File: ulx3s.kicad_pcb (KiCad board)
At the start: 4 copper layers, 94 x 50.8 mm, 164 parts, among them J3 WIFI_OFF, J4 CONN_02X03, Q1 BC857, Q2 2N7002, U10 IS25LP128F-JBLE, U11 PCA9306D, U3 TLV62569DBV, U4 TLV62569DBV, U5 TLV62569DBV, U7 MCP7940NT, Y2 32768Hz

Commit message: full breakout
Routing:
- net Net-(U1-PadD11): track 0.00 -> 3.33 mm, vias 0 -> 1
- net Net-(U1-PadD10): track 0.00 -> 3.17 mm, vias 0 -> 1
- net +3V3: track 14.5 -> 12.0 mm
- net FPDI_SCL: track 6.41 -> 4.93 mm
- net GND: track 23.8 -> 22.4 mm
- net GN27: track 5.26 -> 4.13 mm
- net 2V5_3V3: track 4.11 -> 3.06 mm
- net +1V1: track 13.6 -> 14.5 mm, vias 11 -> 13
- net WIFI_GPIO25: track 4.93 -> 5.73 mm
- net GN0: track 3.17 -> 2.37 mm
- net +2V5: track 6.93 -> 6.18 mm
- net SW4: track 4.81 -> 4.13 mm
- net Net-(U1-PadE11): track 4.81 -> 4.13 mm

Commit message: finishing touches to bga breakout
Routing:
- net +3V3: track 12.0 -> 7.48 mm
- net Net-(U1-PadR3): track 0.00 -> 2.77 mm, vias 0 -> 1
- net ADC_MOSI: track 5.25 -> 6.39 mm
- net SD_WP: track 5.66 -> 4.54 mm
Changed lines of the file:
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@@
     (thickness 1.6)
     (drawings 5)
-    (tracks 810)
+    (tracks 806)
     (zones 0)
     (modules 228)
@@
   )
   (setup
-    (last_trace_width 0.4)
+    (last_trace_width 0.127)
     (user_trace_width 0.127)
     (user_trace_width 0.2)
@@
   )
   (module Capacitor_SMD:C_0603_1608Metric (layer B.Cu)
-    (at 131.08 95.175 270)
+    (at 131.28 95.175 270)
     (descr "Capacitor SMD 0603 (1608 Metric), square (rectangular) end terminal, IPC_7351 nominal, (Body size source: IPC-SM-782 page 76, https://www.pcb-3d.com/wordpress/wp-content/uploads/ipc-sm-782a_amendment_1_and_2.pdf), generated with kicad-footprint-generator")
     (tags capacitor)
@@
   (via (at 134.88 91.4) (size 0.419) (drill 0.2) (layers F.Cu B.Cu) (net 1))
   (segment (start 134.88 90.75) (end 134.88 91.4) (width 0.2) (layer B.Cu) (net 1))
-  (via (at 130.88 96.6) (size 0.419) (drill 0.2) (layers F.Cu B.Cu) (net 1))
   (via (at 135.68 96.2) (size 0.419) (drill 0.2) (layers F.Cu B.Cu) (net 1))
   (via (at 136.48 96) (size 0.419) (drill 0.2) (layers F.Cu B.Cu) (net 1))
@@
   (segment (start 132.88 95.6) (end 133.28 96) (width 0.4) (layer B.Cu) (net 1))
   (segment (start 132.88 95.375) (end 132.88 95.6) (width 0.4) (layer B.Cu) (net 1))
-  (segment (start 131.08 96.4) (end 130.88 96.6) (width 0.4) (layer B.Cu) (net 1))
-  (segment (start 131.08 95.95) (end 131.08 96.4) (width 0.4) (layer B.Cu) (net 1))
   (segment (start 135.23 95.75) (end 135.68 96.2) (width 0.4) (layer B.Cu) (net 1))
   (segment (start 134.88 95.75) (end 135.23 95.75) (width 0.4) (layer B.Cu) (net 1))
@@
   (segment (start 136.88 95.375) (end 136.88 95.6) (width 0.4) (layer B.Cu) (net 1))
   (segment (start 132.08 90.2) (end 132.48 90.6) (width 0.4) (layer F.Cu) (net 1))
+  (via (at 131.68 96.6) (size 0.419) (drill 0.2) (layers F.Cu B.Cu) (net 1))
+  (segment (start 131.28 96.2) (end 131.68 96.6) (width 0.4) (layer B.Cu) (net 1))
+  (segment (start 131.28 95.95) (end 131.28 96.2) (width 0.4) (layer B.Cu) (net 1))
   (via (at 134.08 93) (size 0.419) (drill 0.2) (layers F.Cu B.Cu) (net 5))
   (via (at 131.68 91.4) (size 0.419) (drill 0.2) (layers F.Cu B.Cu) (net 5))
@@
   (segment (start 128.48 95.4) (end 128.88 95) (width 0.2) (layer F.Cu) (net 5))
   (segment (start 128.08 95.8) (end 128.48 95.4) (width 0.2) (layer F.Cu) (net 5))
-  (via (at 128.48 95.4) (size 0.419) (drill 0.2) (layers F.Cu B.Cu) (net 5))
-  (segment (start 130.995338 93.54799) (end 131.48 93.063328) (width 0.2) (layer B.Cu) (net 5))
-  (segment (start 130.781968 93.54799) (end 130.995338 93.54799) (width 0.2) (layer B.Cu) (net 5))
-  (segment (start 130.60613 93.372152) (end 130.781968 93.54799) (width 0.2) (layer B.Cu) (net 5))
-  (segment (start 129.879132 93.372152) (end 130.60613 93.372152) (width 0.2) (layer B.Cu) (net 5))
-  (segment (start 128.48352 94.767764) (end 129.879132 93.372152) (width 0.2) (layer B.Cu) (net 5))
-  (segment (start 128.48352 95.39648) (end 128.48352 94.767764) (width 0.2) (layer B.Cu) (net 5))
-  (segment (start 128.48 95.4) (end 128.48352 95.39648) (width 0.2) (layer B.Cu) (net 5))
   (segment (start 135.68 87.6) (end 135.68 87.4) (width 0.2) (layer B.Cu) (net 5))
   (segment (start 134.88 88.85) (end 134.88 88.4) (width 0.2) (layer B.Cu) (net 5))
@@
   (segment (start 131.28 91.8) (end 132.08 91) (width 0.2) (layer F.Cu) (net 5))
   (segment (start 131.28 91) (end 131.68 91.4) (width 0.2) (layer F.Cu) (net 5))
+  (via (at 128.48 95.4) (size 0.419) (drill 0.2) (layers F.Cu B.Cu) (net 5))
   (segment (start 127.28 96.6) (end 126.28 96.6) (width 0.127) (layer F.Cu) (net 6))
   (segment (start 127.28 94.2) (end 126.28 94.2) (width 0.127) (layer F.Cu) (net 7))
@@
   (via (at 130.08 95.4) (size 0.419) (drill 0.2) (layers F.Cu B.Cu) (net 19))
   (segment (start 130.48 95) (end 130.08 95.4) (width 0.127) (layer F.Cu) (net 19))
-  (segment (start 130.08 95.4) (end 130.08 99.2) (width 0.127) (layer B.Cu) (net 19))
+  (segment (start 130.08 95.4) (end 130.08 99.2) (width 0.127) (layer In2.Cu) (net 19))
   (segment (start 130.070501 96.209499) (end 130.070501 99.190501) (width 0.127) (layer F.Cu) (net 20))
   (segment (start 130.48 95.8) (end 130.070501 96.209499) (width 0.127) (layer F.Cu) (net 20))
@@
   (segment (start 139.670501 96.190501) (end 139.670501 99.190501) (width 0.127) (layer F.Cu) (net 140))
   (segment (start 139.28 95.8) (end 139.670501 96.190501) (width 0.127) (layer F.Cu) (net 140))
-  (via (at 139.679999 94.6) (size 0.419) (drill 0.2) (layers F.Cu B.Cu) (net 141))
-  (segment (start 139.28 94.200001) (end 139.679999 94.6) (width 0.127) (layer F.Cu) (net 141))
   (segment (start 139.28 94.2) (end 139.28 94.200001) (width 0.127) (layer F.Cu) (net 141))
+  (segment (start 139.28 94.200001) (end 139.679999 94.6) (width 0.127) (layer F.Cu) (net 141))
+  (via (at 139.679999 94.6) (size 0.419) (drill 0.2) (layers F.Cu B.Cu) (net 141))
+  (segment (start 137.68 95.58766) (end 137.68 99) (width 0.127) (layer B.Cu) (net 141))
+  (segment (start 138.06766 95.2) (end 137.68 95.58766) (width 0.127) (layer B.Cu) (net 141))
+  (segment (start 139.08 95.2) (end 138.06766 95.2) (width 0.127) (layer B.Cu) (net 141))
+  (segment (start 139.679999 94.600001) (end 139.08 95.2) (width 0.127) (layer B.Cu) (net 141))
   (segment (start 139.679999 94.6) (end 139.679999 94.600001) (width 0.127) (layer B.Cu) (net 141))
-  (segment (start 139.679999 94.600001) (end 139.48 94.8) (width 0.127) (layer B.Cu) (net 141))
-  (segment (start 139.48 94.8) (end 139.48 99.2) (width 0.127) (layer B.Cu) (net 141))
   (via (at 140.48 94.6) (size 0.419) (drill 0.2) (layers F.Cu B.Cu) (net 142))
   (segment (start 140.08 94.2) (end 140.48 94.6) (width 0.127) (layer F.Cu) (net 142))
@@
   (via (at 139.68 93.8) (size 0.419) (drill 0.2) (layers F.Cu B.Cu) (net 143))
   (segment (start 140.08 93.4) (end 139.68 93.8) (width 0.127) (layer F.Cu) (net 143))
-  (segment (start 139.73401 98.14599) (end 139.73401 99.05401) (width 0.127) (layer B.Cu) (net 143))
-  (segment (start 139.73401 95.14599) (end 139.73401 98.14599) (width 0.127) (layer B.Cu) (net 143))
-  (segment (start 140.079999 94.800001) (end 139.73401 95.14599) (width 0.127) (layer B.Cu) (net 143))
   (segment (start 140.079999 94.200001) (end 140.079999 94.800001) (width 0.127) (layer B.Cu) (net 143))
   (segment (start 139.68 93.8) (end 140.079999 94.200001) (width 0.127) (layer B.Cu) (net 143))
+  (segment (start 140.079999 94.874069) (end 139.68 95.274068) (width 0.127) (layer B.Cu) (net 143))
+  (segment (start 140.079999 94.800001) (end 140.079999 94.874069) (width 0.127) (layer B.Cu) (net 143))
+  (segment (start 139.68 95.274068) (end 139.68 98.8) (width 0.127) (layer B.Cu) (net 143))
   (via (at 131.68 85) (size 0.419) (drill 0.2) (layers F.Cu B.Cu) (net 144))
   (segment (start 132.08 85.4) (end 131.68 85) (width 0.127) (layer F.Cu) (net 144))
@@
   (segment (start 139.292371 94.387629) (end 139.48 94.2) (width 0.127) (layer In2.Cu) (net 275))
   (segment (start 139.48 94.2) (end 143.28 94.2) (width 0.127) (layer In2.Cu) (net 275))
+  (via (at 128.48 94.6) (size 0.419) (drill 0.2) (layers F.Cu B.Cu) (net 276))
+  (segment (start 128.88 94.2) (end 128.48 94.6) (width 0.127) (layer F.Cu) (net 276))
+  (segment (start 128.48 94.6) (end 126.28 94.6) (width 0.127) (layer B.Cu) (net 276))
   (via (at 130.088653 93.808653) (size 0.419) (drill 0.2) (layers F.Cu B.Cu) (net 277))
   (segment (start 130.48 93.417306) (end 130.088653 93.808653) (width 0.127) (layer F.Cu) (net 277))
   (segment (start 130.48 93.4) (end 130.48 93.417306) (width 0.127) (layer F.Cu) (net 277))
-  (segment (start 130.088653 93.808653) (end 129.68 94.217306) (width 0.127) (layer B.Cu) (net 277))
-  (segment (start 129.68 94.217306) (end 129.68 95) (width 0.127) (layer B.Cu) (net 277))
-  (segment (start 129.68 95) (end 128.88 95.8) (width 0.127) (layer B.Cu) (net 277))
-  (segment (start 128.88 95.8) (end 126.28 95.8) (width 0.127) (layer B.Cu) (net 277))
+  (segment (start 130.088653 93.808653) (end 129.697306 94.2) (width 0.127) (layer B.Cu) (net 277))
+  (segment (start 129.697306 94.2) (end 126.28 94.2) (width 0.127) (layer B.Cu) (net 277))
   (via (at 130.88 93) (size 0.419) (drill 0.2) (layers F.Cu B.Cu) (net 278))
   (segment (start 130.48 92.6) (end 130.88 93) (width 0.127) (layer F.Cu) (net 278))
@@
     (polygon
       (pts
-        (xy 137.88 87.6) (xy 139.48 87.6) (xy 139.48 93.2) (xy 134.88 93.2) (xy 133.48 93.2)
-        (xy 131.08 93.2) (xy 131.08 90.6) (xy 134.68 90.6) (xy 134.68 87.2) (xy 137.88 87.2)
+        (xy 137.88 87.6) (xy 139.48 87.6) (xy 139.48 96) (xy 134.88 96) (xy 133.48 96)
+        (xy 128.08 96) (xy 128.08 90.6) (xy 134.68 90.6) (xy 134.68 87.2) (xy 137.88 87.2)
       )
     )

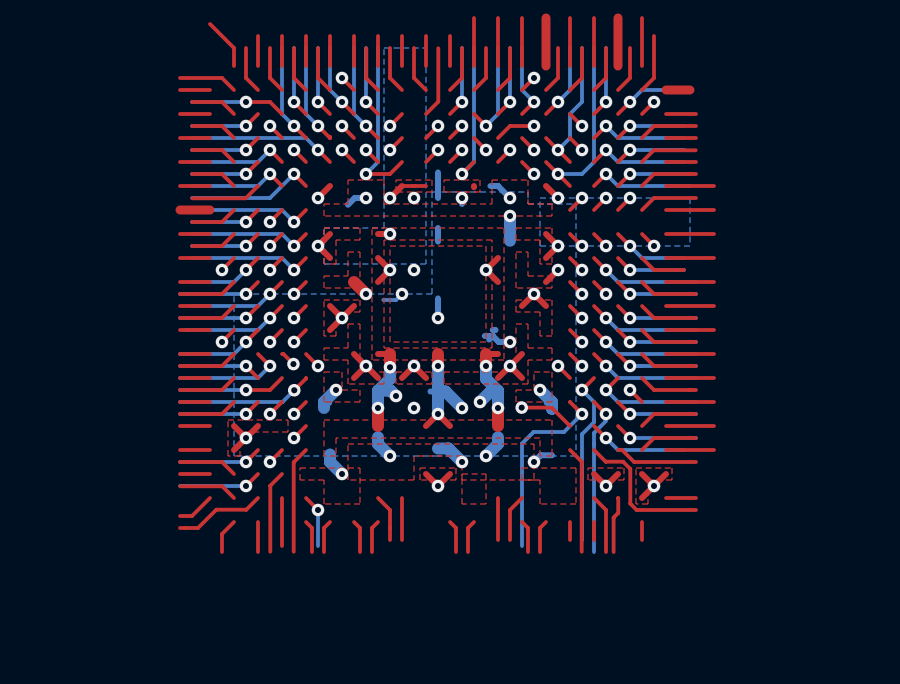
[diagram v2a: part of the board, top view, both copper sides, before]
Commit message: replace most top layer fills with traces
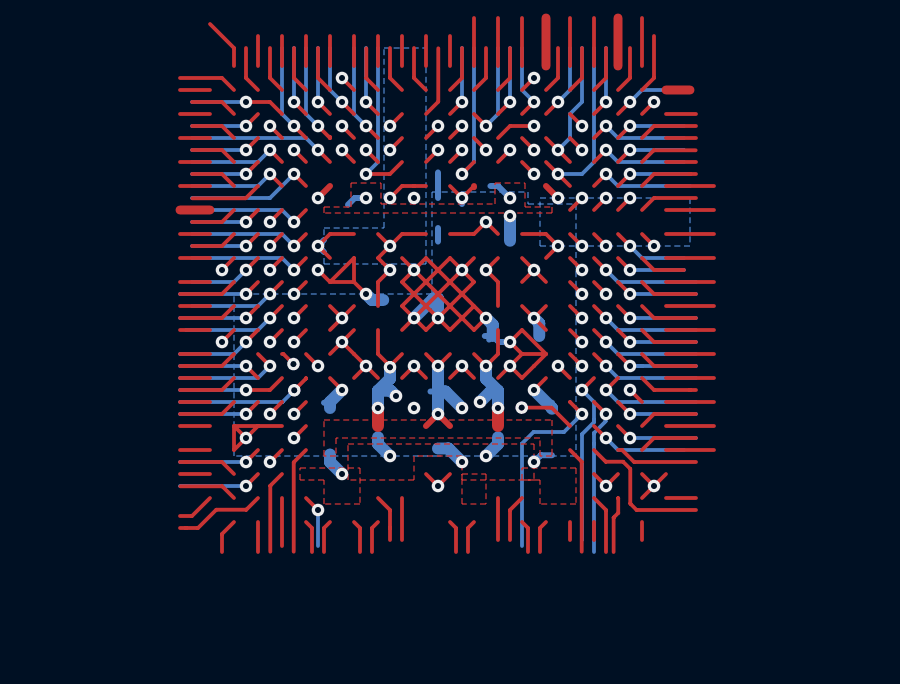
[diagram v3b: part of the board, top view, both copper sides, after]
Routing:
- net GND: track 22.5 -> 57.2 mm, vias 30 -> 35
- net +1V1: track 14.5 -> 23.1 mm, vias 13 -> 14
- net +3V3: track 7.48 -> 13.1 mm
- net +2V5: track 6.18 -> 7.36 mm
- net 2V5_3V3: track 3.06 -> 3.86 mm
- removed copper zone on F.Cu, net +2V5
- removed copper zone on F.Cu, net +3V3
- removed copper zone on F.Cu, net 2V5_3V3

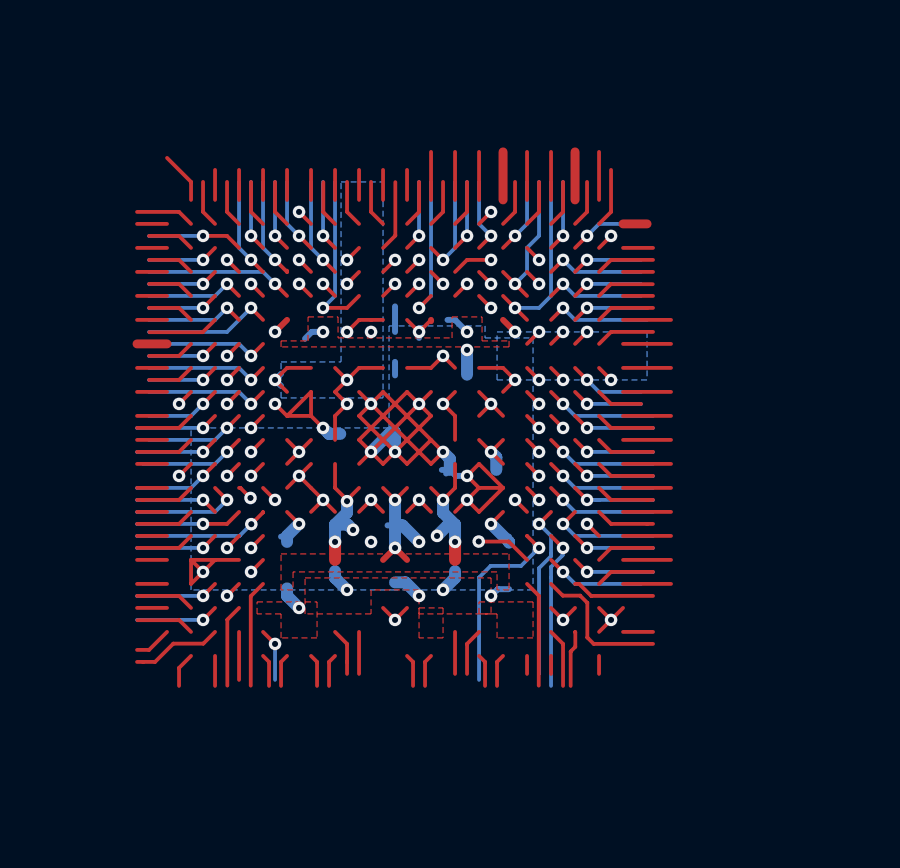
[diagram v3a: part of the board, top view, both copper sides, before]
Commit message: convert top layer pours to traces
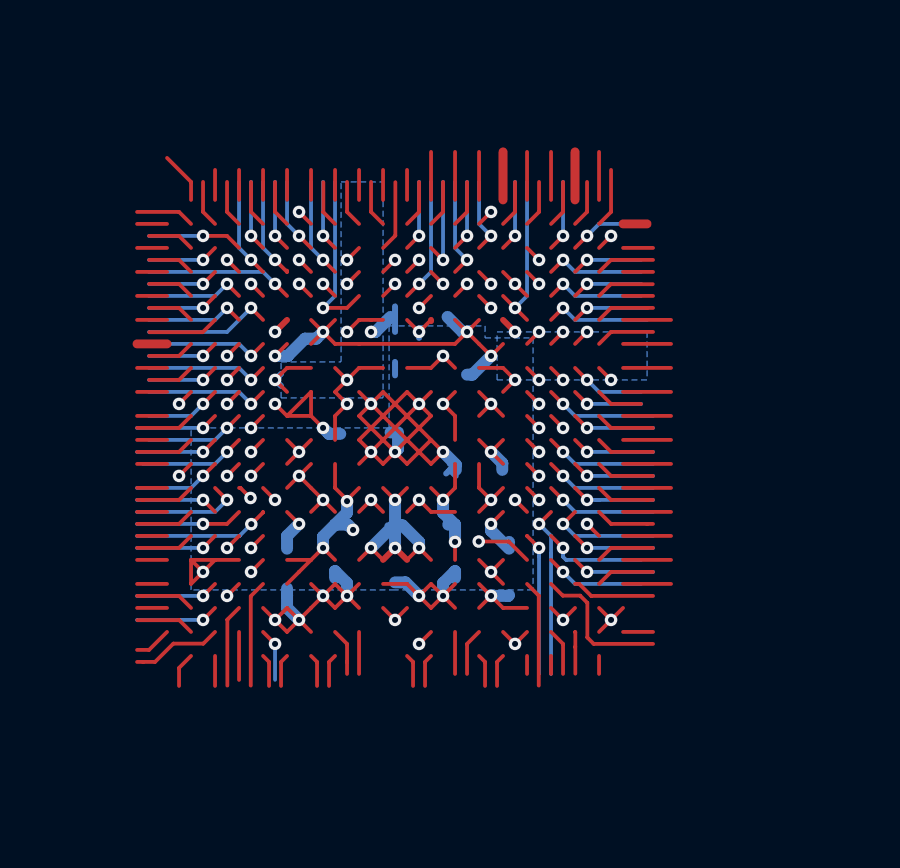
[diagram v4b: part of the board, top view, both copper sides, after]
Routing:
- net GND: track 57.2 -> 83.5 mm, vias 35 -> 39
- net +1V1: track 23.1 -> 30.7 mm
- net ADC_CSn: track 5.33 -> 3.53 mm
- net ADC_MOSI: track 6.39 -> 4.77 mm
- net +2V5: track 7.36 -> 8.32 mm
- net USB_FPGA_D-: track 6.30 -> 5.50 mm
- net GP27: track 4.13 -> 3.33 mm
- net FPDI_SCL: track 4.93 -> 5.53 mm
- removed copper zone on F.Cu, net +1V1
- removed copper zone on F.Cu, net GND
